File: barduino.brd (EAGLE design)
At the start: 68.5 x 37.2 mm, 14 parts, among them Q2 16MHz, X1 MINI-USB-UX60A-MB-5ST

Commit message: remove VCC resistor
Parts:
- moved X1 2.37 mm to (-14.6, 32.0)
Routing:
- net VCC: track 133.1 -> 110.4 mm
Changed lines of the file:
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@@
 <attribute name="OC_NEWARK" value="unknown" x="-5.989321875" y="43.5432125" size="1.778" layer="27" rot="R90" display="off"/>
-</element>
-<element name="X1" library="con-hirose" library_urn="urn:adsk.eagle:library:152" package="UX60A-MB-5ST" value="MINI-USB-UX60A-MB-5ST" x="-16.289015625" y="30.31998125">
-<attribute name="MF" value="" x="-16.289015625" y="30.31998125" size="1.778" layer="27" display="off"/>
-<attribute name="MPN" value="" x="-16.289015625" y="30.31998125" size="1.778" layer="27" display="off"/>
-<attribute name="OC_FARNELL" value="unknown" x="-16.289015625" y="30.31998125" size="1.778" layer="27" display="off"/>
-<attribute name="OC_NEWARK" value="unknown" x="-16.289015625" y="30.31998125" size="1.778" layer="27" display="off"/>
 </element>
 <element name="S1" library="ng" package="6MM_SWITCH" value="MIN" x="25.181559375" y="47.762159375" rot="R90"/>
 <element name="U$2" library="4-Digit-Clock" package="HEADER" value="HEADER" x="10.8103" y="36.7183"/>
 <element name="U$3" library="4-Digit-Clock" package="HEADER" value="HEADER" x="10.8103" y="21.4783" rot="R180"/>
+<element name="X1" library="con-hirose" package="UX60A-MB-5ST" value="MINI-USB-UX60A-MB-5ST" x="-14.5796" y="31.9659">
+<attribute name="MF" value="" x="-14.5796" y="31.9659" size="1.778" layer="27" display="off"/>
+<attribute name="MPN" value="" x="-14.5796" y="31.9659" size="1.778" layer="27" display="off"/>
+<attribute name="OC_FARNELL" value="unknown" x="-14.5796" y="31.9659" size="1.778" layer="27" display="off"/>
+<attribute name="OC_NEWARK" value="unknown" x="-14.5796" y="31.9659" size="1.778" layer="27" display="off"/>
+</element>
 </elements>
 <signals>
@@
 <wire x1="9.244540625" y1="27.8983" x2="6.5177" y2="27.8983" width="0.4064" layer="1"/>
 <wire x1="9.244540625" y1="27.8983" x2="9.922509375" y2="28.57626875" width="0.4064" layer="1"/>
-<wire x1="4.220421875" y1="27.8983" x2="6.5177" y2="27.8983" width="0.4064" layer="1"/>
-<contactref element="X1" pad="1"/>
-<wire x1="-14.039015625" y1="31.91998125" x2="-13.111678125" y2="31.91998125" width="0.4064" layer="1"/>
-<wire x1="-13.111678125" y1="31.91998125" x2="-12.065" y2="32.966659375" width="0.4064" layer="1"/>
-<wire x1="-12.065" y1="36.86048125" x2="-12.065" y2="32.966659375" width="0.4064" layer="1"/>
-<wire x1="-12.065" y1="36.86048125" x2="-20.460621875" y2="36.86048125" width="0.4064" layer="1"/>
-<wire x1="-20.460621875" y1="36.86048125" x2="-22.892215625" y2="34.4288875" width="0.4064" layer="1"/>
-<wire x1="-9.3187" y1="18.72916875" x2="-8.96160625" y2="18.372075" width="0.4064" layer="1"/>
-<wire x1="-8.96160625" y1="18.372075" x2="-6.85659375" y2="18.372075" width="0.4064" layer="1"/>
-<wire x1="-6.608340625" y1="27.8855" x2="-6.273253125" y2="27.88484375" width="0.4064" layer="1"/>
-<wire x1="-6.273253125" y1="27.88484375" x2="-6.27259375" y2="27.8855" width="0.4064" layer="1"/>
-<wire x1="-6.27259375" y1="27.8855" x2="4.220421875" y2="27.8855" width="0.4064" layer="1"/>
-<wire x1="-6.4868" y1="27.763959375" x2="-6.608340625" y2="27.8855" width="0.4064" layer="1"/>
-<wire x1="-22.892215625" y1="26.211075" x2="-20.941521875" y2="24.26038125" width="0.4064" layer="1"/>
-<wire x1="-6.85659375" y1="18.372075" x2="-6.4868" y2="18.74186875" width="0.4064" layer="1"/>
-<wire x1="-6.4868" y1="18.74186875" x2="-6.4868" y2="27.763959375" width="0.4064" layer="1"/>
-<wire x1="-20.941521875" y1="24.26038125" x2="-9.3187" y2="24.237621875" width="0.4064" layer="1"/>
-<wire x1="-9.3187" y1="24.237621875" x2="-9.3187" y2="18.72916875" width="0.4064" layer="1"/>
-<wire x1="-22.892215625" y1="34.4288875" x2="-22.892215625" y2="26.211075" width="0.4064" layer="1"/>
 <contactref element="R3" pad="2"/>
 <wire x1="7.404440625" y1="47.919625" x2="-2.646665625" y2="47.919625" width="0.4064" layer="1"/>
@@
 <wire x1="-10.024109375" y1="48.258728125" x2="-10.18031875" y2="48.10251875" width="0.4064" layer="1"/>
 <wire x1="-10.18031875" y1="48.10251875" x2="-10.1117375" y2="48.10251875" width="0.4064" layer="1"/>
-<wire x1="-10.024109375" y1="48.258728125" x2="-10.024109375" y2="38.901371875" width="0.4064" layer="1"/>
-<wire x1="-10.024109375" y1="38.901371875" x2="-12.065" y2="36.86048125" width="0.4064" layer="1"/>
-<wire x1="4.220421875" y1="27.8855" x2="4.220421875" y2="27.8983" width="0" layer="19" extent="1-1"/>
+<contactref element="X1" pad="1"/>
+<wire x1="-2.698959375" y1="27.8983" x2="6.5177" y2="27.8983" width="0.4064" layer="1"/>
+<wire x1="-10.099040625" y1="33.5659" x2="-12.3296" y2="33.5659" width="0.4064" layer="1"/>
+<wire x1="-10.024109375" y1="33.64083125" x2="-10.099040625" y2="33.5659" width="0.4064" layer="1"/>
+<wire x1="-10.024109375" y1="48.258728125" x2="-10.024109375" y2="33.64083125" width="0.4064" layer="1"/>
+<wire x1="-12.3296" y1="33.5659" x2="-14.564559375" y2="33.5659" width="0.4064" layer="1"/>
+<wire x1="-14.564559375" y1="33.5659" x2="-14.594840625" y2="33.53561875" width="0.4064" layer="1"/>
+<wire x1="-14.594840625" y1="33.53561875" x2="-14.594840625" y2="23.497540625" width="0.4064" layer="1"/>
+<wire x1="-14.594840625" y1="23.497540625" x2="-9.12621875" y2="18.02891875" width="0.4064" layer="1"/>
+<wire x1="-9.12621875" y1="18.02891875" x2="-7.0586625" y2="18.02891875" width="0.4064" layer="1"/>
+<wire x1="-7.0586625" y1="18.02891875" x2="-6.58368125" y2="18.5039" width="0.4064" layer="1"/>
+<wire x1="-6.58368125" y1="18.5039" x2="-6.497321875" y2="18.6195875" width="0.4064" layer="1"/>
+<wire x1="-6.4868" y1="26.3325375" x2="-4.87171875" y2="27.899359375" width="0.4064" layer="1"/>
+<wire x1="-6.497321875" y1="18.6195875" x2="-6.4868" y2="18.74186875" width="0.4064" layer="1"/>
+<wire x1="-6.4868" y1="18.74186875" x2="-6.4868" y2="26.3325375" width="0.4064" layer="1"/>
+<wire x1="-4.87171875" y1="27.899359375" x2="-2.748278125" y2="27.899359375" width="0.4064" layer="1"/>
+<wire x1="-2.748278125" y1="27.899359375" x2="-2.698959375" y2="27.8983" width="0.4064" layer="1"/>
 </signal>
 <signal name="GND" class="1">
@@
 <contactref element="C5" pad="1"/>
 <contactref element="SG1" pad="-"/>
-<contactref element="X1" pad="5"/>
 <contactref element="C2" pad="1"/>
 <contactref element="ICSP" pad="6"/>
@@
 <wire x1="36.062978125" y1="44.452603125" x2="36.062978125" y2="42.3317" width="0.4064" layer="1"/>
 <wire x1="36.062978125" y1="42.3317" x2="29.94151875" y2="36.210240625" width="0.4064" layer="1"/>
-<wire x1="-6.6083375" y1="28.6983" x2="-8.17528125" y2="28.70136875" width="0.4064" layer="1"/>
-<wire x1="-8.17528125" y1="28.70136875" x2="-10.304521875" y2="28.7055375" width="0.4064" layer="1"/>
-<wire x1="-7.9091" y1="19.883175" x2="-7.9091" y2="24.41708125" width="0.4064" layer="1"/>
+<wire x1="-7.9091" y1="24.41708125" x2="-7.9091" y2="19.883175" width="0.4064" layer="1"/>
 <wire x1="-7.9091" y1="24.41708125" x2="-7.8964" y2="24.42978125" width="0.4064" layer="1"/>
-<wire x1="-7.8964" y1="24.42978125" x2="-7.8964" y2="28.4224875" width="0.4064" layer="1"/>
-<wire x1="-7.8964" y1="28.4224875" x2="-8.17528125" y2="28.70136875" width="0.4064" layer="1"/>
 <contactref element="U$1" pad="21"/>
 <contactref element="U$1" pad="3"/>
 <contactref element="U$1" pad="5"/>
 <contactref element="C7" pad="1"/>
-<wire x1="6.5177" y1="28.6983" x2="-6.6083375" y2="28.6983" width="0.4064" layer="1"/>
 <wire x1="11.218" y1="30.2983" x2="6.5177" y2="30.2983" width="0.4064" layer="1"/>
 <wire x1="12.049759375" y1="29.466540625" x2="11.218" y2="30.2983" width="0.4064" layer="1"/>
@@
 <wire x1="19.705265625" y1="29.849740625" x2="19.705265625" y2="30.512965625" width="0.4064" layer="1"/>
 <wire x1="19.705265625" y1="30.512965625" x2="26.083259375" y2="36.890959375" width="0.4064" layer="1"/>
-<wire x1="6.5177" y1="30.2983" x2="5.32248125" y2="30.2983" width="0.4064" layer="1"/>
-<wire x1="5.32248125" y1="30.2983" x2="4.64058125" y2="29.6164" width="0.4064" layer="1"/>
-<wire x1="4.64058125" y1="29.6164" x2="4.64058125" y2="28.71110625" width="0.4064" layer="1"/>
+<wire x1="4.64058125" y1="30.177740625" x2="4.64058125" y2="30.4626875" width="0.4064" layer="1"/>
+<wire x1="4.64058125" y1="30.177740625" x2="4.64058125" y2="28.71110625" width="0.4064" layer="1"/>
 <wire x1="3.55945" y1="31.54381875" x2="2.200071875" y2="31.54381875" width="0.4064" layer="1"/>
 <wire x1="2.200071875" y1="31.54381875" x2="-5.989321875" y2="39.7332125" width="0.4064" layer="1"/>
-<wire x1="4.64058125" y1="29.6164" x2="4.64058125" y2="30.4626875" width="0.4064" layer="1"/>
 <wire x1="4.64058125" y1="30.4626875" x2="3.55945" y2="31.54381875" width="0.4064" layer="1"/>
-<wire x1="-10.304521875" y1="28.7055375" x2="-12.741353125" y2="28.7055375" width="0.4064" layer="1"/>
-<wire x1="-12.741353125" y1="28.7055375" x2="-12.786509375" y2="28.66038125" width="0.4064" layer="1"/>
-<wire x1="-12.786509375" y1="28.66038125" x2="-14.039015625" y2="28.66038125" width="0.4064" layer="1"/>
-<wire x1="6.5177" y1="28.6983" x2="6.5177" y2="30.2983" width="0" layer="19" extent="1-1"/>
-<wire x1="-14.039015625" y1="28.71998125" x2="-14.039015625" y2="28.66038125" width="0" layer="19" extent="1-1"/>
+<contactref element="X1" pad="5"/>
+<wire x1="6.5177" y1="28.6983" x2="4.6533875" y2="28.6983" width="0.4064" layer="1"/>
+<wire x1="4.6533875" y1="28.6983" x2="4.64058125" y2="28.71110625" width="0.4064" layer="1"/>
+<wire x1="4.80496875" y1="30.2983" x2="4.64058125" y2="30.4626875" width="0.4064" layer="1"/>
+<wire x1="6.5177" y1="30.2983" x2="4.80496875" y2="30.2983" width="0.4064" layer="1"/>
+<wire x1="-8.016240625" y1="30.3659" x2="-12.3296" y2="30.3659" width="0.4064" layer="1"/>
+<wire x1="-8.016240625" y1="30.3659" x2="4.452421875" y2="30.3659" width="0.4064" layer="1"/>
+<wire x1="4.452421875" y1="30.3659" x2="4.64058125" y2="30.177740625" width="0.4064" layer="1"/>
+<wire x1="-7.8964" y1="24.42978125" x2="-7.8964" y2="30.246059375" width="0.4064" layer="1"/>
+<wire x1="-7.8964" y1="30.246059375" x2="-8.016240625" y2="30.3659" width="0.4064" layer="1"/>
 </signal>
 <signal name="PB7">

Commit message: put new buzzer on board
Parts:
- removed SG1: F/CM12P, buzzer:F/CM12P
- added U$4: BUZZER, 4-Digit-Clock:BUZZER
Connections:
- net D3: now also U$4.P$1; no longer SG1.+
- net GND: now also U$4.P$2; no longer SG1.-
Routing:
- net D3: track 21.4 -> 13.8 mm
- net VCC: track 110.4 -> 104.8 mm
- net GND: track 102.8 -> 99.7 mm
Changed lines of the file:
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@@
 <element name="U$1" library="fab" package="TQFP32-08THIN" value="ATMEGA88-THIN" x="10.8103" y="29.0983"/>
 <element name="ICSP" library="fab" package="2X03SMD" value="PROG" x="28.514096875" y="27.335546875" rot="R90"/>
-<element name="SG1" library="buzzer" library_urn="urn:adsk.eagle:library:113" package="F/CM12P" value="F/CM12P" x="-5.989321875" y="43.5432125" rot="R90">
-<attribute name="MF" value="" x="-5.989321875" y="43.5432125" size="1.778" layer="27" rot="R90" display="off"/>
-<attribute name="MPN" value="" x="-5.989321875" y="43.5432125" size="1.778" layer="27" rot="R90" display="off"/>
-<attribute name="OC_FARNELL" value="unknown" x="-5.989321875" y="43.5432125" size="1.778" layer="27" rot="R90" display="off"/>
-<attribute name="OC_NEWARK" value="unknown" x="-5.989321875" y="43.5432125" size="1.778" layer="27" rot="R90" display="off"/>
-</element>
 <element name="S1" library="ng" package="6MM_SWITCH" value="MIN" x="25.181559375" y="47.762159375" rot="R90"/>
 <element name="U$2" library="4-Digit-Clock" package="HEADER" value="HEADER" x="10.8103" y="36.7183"/>
@@
 <attribute name="OC_NEWARK" value="unknown" x="-14.5796" y="31.9659" size="1.778" layer="27" display="off"/>
 </element>
+<element name="U$4" library="4-Digit-Clock" package="BUZZER" value="BUZZER" x="-1.541778125" y="42.10558125" rot="R180"/>
 </elements>
 <signals>
@@
 <wire x1="9.244540625" y1="27.8983" x2="9.922509375" y2="28.57626875" width="0.4064" layer="1"/>
 <contactref element="R3" pad="2"/>
-<wire x1="7.404440625" y1="47.919625" x2="-2.646665625" y2="47.919625" width="0.4064" layer="1"/>
-<wire x1="-2.646665625" y1="47.919625" x2="-3.959859375" y2="49.23281875" width="0.4064" layer="1"/>
-<wire x1="-3.959859375" y1="49.23281875" x2="-5.2107625" y2="49.23281875" width="0.4064" layer="1"/>
-<wire x1="-5.2107625" y1="49.23281875" x2="-5.210765625" y2="49.232821875" width="0.4064" layer="1"/>
-<wire x1="-5.210765625" y1="49.232821875" x2="-9.050015625" y2="49.232821875" width="0.4064" layer="1"/>
-<wire x1="-9.050015625" y1="49.232821875" x2="-10.024109375" y2="48.258728125" width="0.4064" layer="1"/>
-<wire x1="-10.024109375" y1="48.258728125" x2="-10.18031875" y2="48.10251875" width="0.4064" layer="1"/>
-<wire x1="-10.18031875" y1="48.10251875" x2="-10.1117375" y2="48.10251875" width="0.4064" layer="1"/>
 <contactref element="X1" pad="1"/>
 <wire x1="-2.698959375" y1="27.8983" x2="6.5177" y2="27.8983" width="0.4064" layer="1"/>
-<wire x1="-10.099040625" y1="33.5659" x2="-12.3296" y2="33.5659" width="0.4064" layer="1"/>
-<wire x1="-10.024109375" y1="33.64083125" x2="-10.099040625" y2="33.5659" width="0.4064" layer="1"/>
-<wire x1="-10.024109375" y1="48.258728125" x2="-10.024109375" y2="33.64083125" width="0.4064" layer="1"/>
-<wire x1="-12.3296" y1="33.5659" x2="-14.564559375" y2="33.5659" width="0.4064" layer="1"/>
+<wire x1="-14.564559375" y1="33.5659" x2="-12.3296" y2="33.5659" width="0.4064" layer="1"/>
 <wire x1="-14.564559375" y1="33.5659" x2="-14.594840625" y2="33.53561875" width="0.4064" layer="1"/>
 <wire x1="-14.594840625" y1="33.53561875" x2="-14.594840625" y2="23.497540625" width="0.4064" layer="1"/>
@@
 <wire x1="-4.87171875" y1="27.899359375" x2="-2.748278125" y2="27.899359375" width="0.4064" layer="1"/>
 <wire x1="-2.748278125" y1="27.899359375" x2="-2.698959375" y2="27.8983" width="0.4064" layer="1"/>
+<wire x1="7.404440625" y1="47.919625" x2="-3.11405625" y2="47.919625" width="0.4064" layer="1"/>
+<wire x1="-3.11405625" y1="47.919625" x2="-5.717540625" y2="45.316140625" width="0.4064" layer="1"/>
+<wire x1="-5.717540625" y1="37.886640625" x2="-5.717540625" y2="45.316140625" width="0.4064" layer="1"/>
+<wire x1="-12.3296" y1="33.5659" x2="-10.03828125" y2="33.5659" width="0.4064" layer="1"/>
+<wire x1="-10.03828125" y1="33.5659" x2="-5.717540625" y2="37.886640625" width="0.4064" layer="1"/>
 </signal>
 <signal name="GND" class="1">
 <contactref element="C4" pad="1"/>
 <contactref element="C5" pad="1"/>
-<contactref element="SG1" pad="-"/>
 <contactref element="C2" pad="1"/>
 <contactref element="ICSP" pad="6"/>
@@
 <wire x1="19.705265625" y1="29.849740625" x2="19.705265625" y2="30.512965625" width="0.4064" layer="1"/>
 <wire x1="19.705265625" y1="30.512965625" x2="26.083259375" y2="36.890959375" width="0.4064" layer="1"/>
-<wire x1="4.64058125" y1="30.177740625" x2="4.64058125" y2="30.4626875" width="0.4064" layer="1"/>
 <wire x1="4.64058125" y1="30.177740625" x2="4.64058125" y2="28.71110625" width="0.4064" layer="1"/>
-<wire x1="3.55945" y1="31.54381875" x2="2.200071875" y2="31.54381875" width="0.4064" layer="1"/>
-<wire x1="2.200071875" y1="31.54381875" x2="-5.989321875" y2="39.7332125" width="0.4064" layer="1"/>
-<wire x1="4.64058125" y1="30.4626875" x2="3.55945" y2="31.54381875" width="0.4064" layer="1"/>
 <contactref element="X1" pad="5"/>
 <wire x1="6.5177" y1="28.6983" x2="4.6533875" y2="28.6983" width="0.4064" layer="1"/>
 <wire x1="4.6533875" y1="28.6983" x2="4.64058125" y2="28.71110625" width="0.4064" layer="1"/>
-<wire x1="4.80496875" y1="30.2983" x2="4.64058125" y2="30.4626875" width="0.4064" layer="1"/>
-<wire x1="6.5177" y1="30.2983" x2="4.80496875" y2="30.2983" width="0.4064" layer="1"/>
 <wire x1="-8.016240625" y1="30.3659" x2="-12.3296" y2="30.3659" width="0.4064" layer="1"/>
-<wire x1="-8.016240625" y1="30.3659" x2="4.452421875" y2="30.3659" width="0.4064" layer="1"/>
+<wire x1="-2.87528125" y1="30.3659" x2="-8.016240625" y2="30.3659" width="0.4064" layer="1"/>
+<wire x1="4.452421875" y1="30.3659" x2="-2.87528125" y2="30.3659" width="0.4064" layer="1"/>
 <wire x1="4.452421875" y1="30.3659" x2="4.64058125" y2="30.177740625" width="0.4064" layer="1"/>
 <wire x1="-7.8964" y1="24.42978125" x2="-7.8964" y2="30.246059375" width="0.4064" layer="1"/>
 <wire x1="-7.8964" y1="30.246059375" x2="-8.016240625" y2="30.3659" width="0.4064" layer="1"/>
+<contactref element="U$4" pad="P$2"/>
+<wire x1="-2.811778125" y1="42.10558125" x2="-2.811778125" y2="30.429403125" width="0.4064" layer="1"/>
+<wire x1="-2.811778125" y1="30.429403125" x2="-2.87528125" y2="30.3659" width="0.4064" layer="1"/>
+<wire x1="6.5177" y1="30.2983" x2="4.761140625" y2="30.2983" width="0.4064" layer="1"/>
+<wire x1="4.761140625" y1="30.2983" x2="4.64058125" y2="30.177740625" width="0.4064" layer="1"/>
 </signal>
 <signal name="PB7">
@@
 <signal name="D3">
 <contactref element="U$1" pad="1"/>
-<contactref element="SG1" pad="+"/>
 <wire x1="6.4415" y1="31.8983" x2="5.1069625" y2="31.8983" width="0.4064" layer="1"/>
 <wire x1="5.1069625" y1="31.8983" x2="-0.36321875" y2="37.36848125" width="0.4064" layer="1"/>
-<wire x1="-0.36321875" y1="37.36848125" x2="-0.36321875" y2="41.727109375" width="0.4064" layer="1"/>
-<wire x1="-0.36321875" y1="41.727109375" x2="-5.989321875" y2="47.3532125" width="0.4064" layer="1"/>
+<contactref element="U$4" pad="P$1"/>
+<wire x1="-0.36321875" y1="37.36848125" x2="-0.36321875" y2="42.014140625" width="0.4064" layer="1"/>
+<wire x1="-0.36321875" y1="42.014140625" x2="-0.271778125" y2="42.10558125" width="0.4064" layer="1"/>
 </signal>
 <signal name="D4">
@@
 </board>
 </drawing>
-<compatibility>
-<note version="8.2" severity="warning">
-Since Version 8.2, Eagle supports online libraries. The ids
-of those online libraries will not be understood (or retained)
-with this version.
-</note>
-</compatibility>
 </eagle>

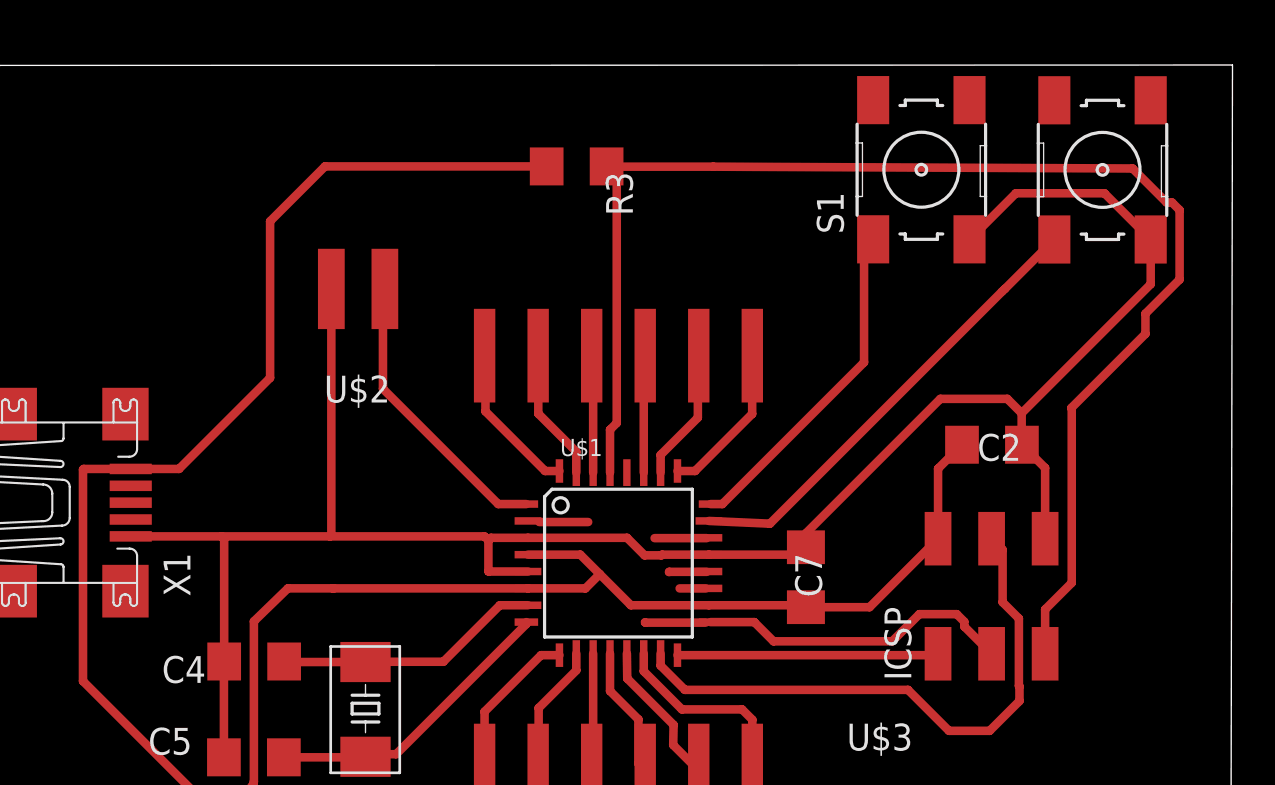
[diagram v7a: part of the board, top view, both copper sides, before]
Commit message: move buttons to top
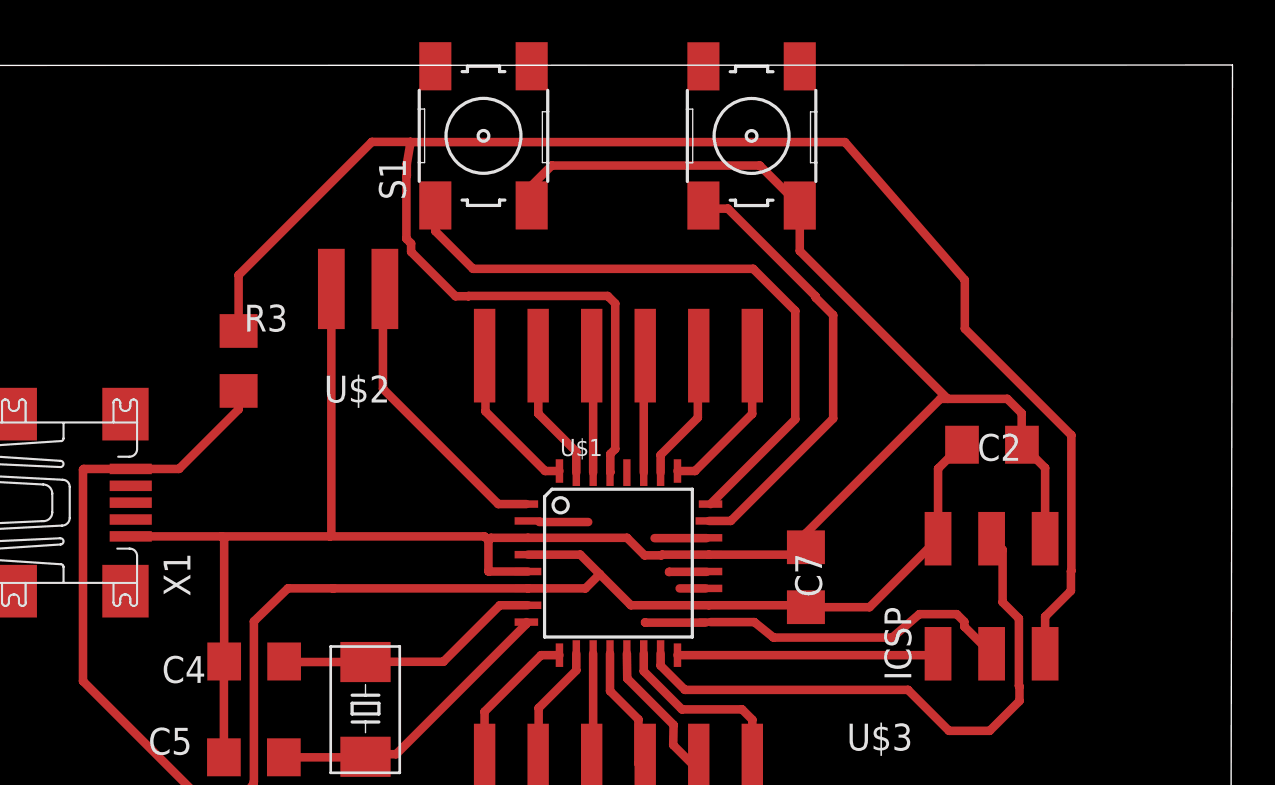
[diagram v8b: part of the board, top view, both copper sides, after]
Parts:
- moved S1 20.8 mm to (4.41, 49.4)
- moved R3 18.5 mm to (-7.21, 38.7), turned to 270 degrees
- moved S0 16.7 mm to (17.1, 49.4)
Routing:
- net VCC: track 104.8 -> 81.9 mm
- net RESET: track 66.4 -> 87.2 mm
- net A1: track 16.1 -> 30.7 mm
- net GND: track 99.7 -> 105.5 mm
- net A0: track 22.0 -> 21.2 mm
